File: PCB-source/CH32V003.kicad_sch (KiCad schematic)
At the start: 5 parts, among them J5 Conn_01x03_Pin, U7 CH32V003FxUx

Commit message: Component placement done
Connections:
- no-connect marks 10 -> 11
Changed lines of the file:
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@@
+	)
+	(no_connect
+		(at 147.32 83.82)
 	)
 	(no_connect

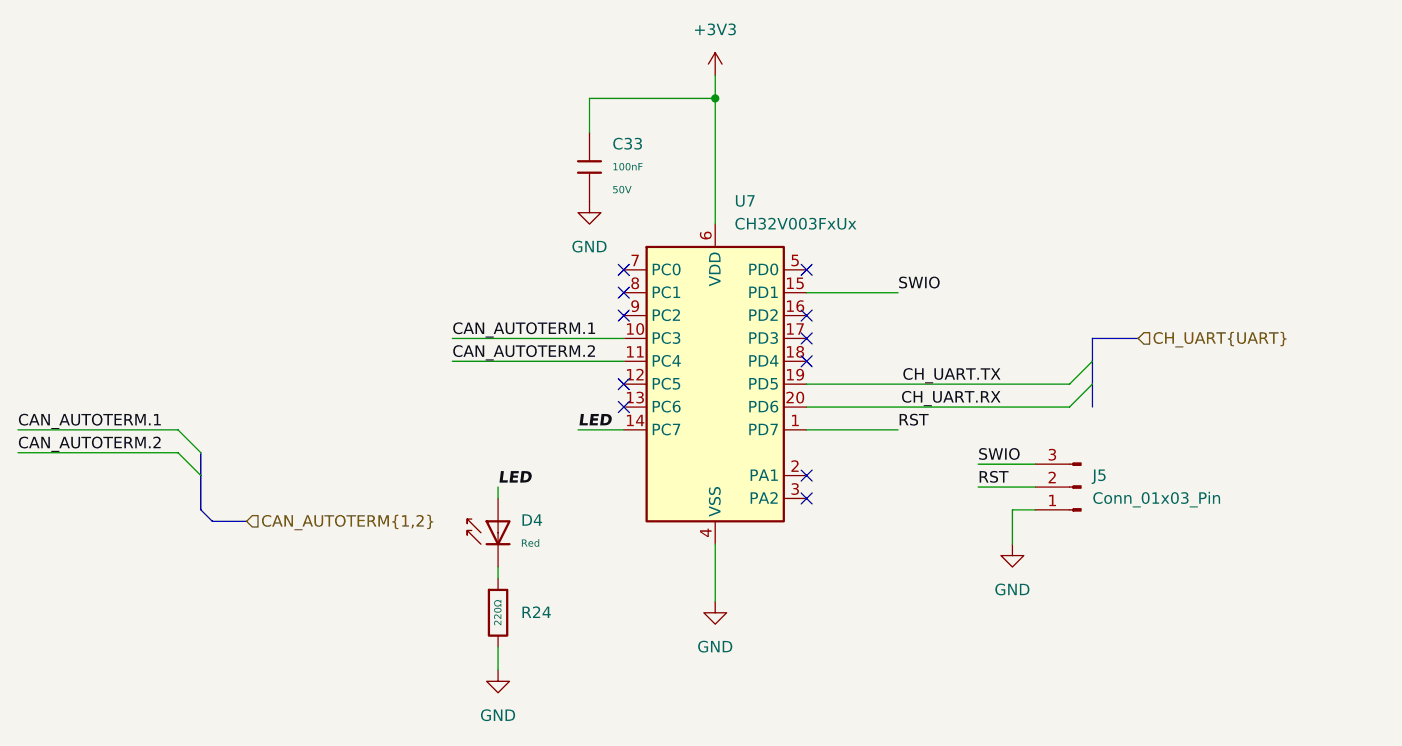
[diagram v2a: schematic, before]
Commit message: change can term add usr led
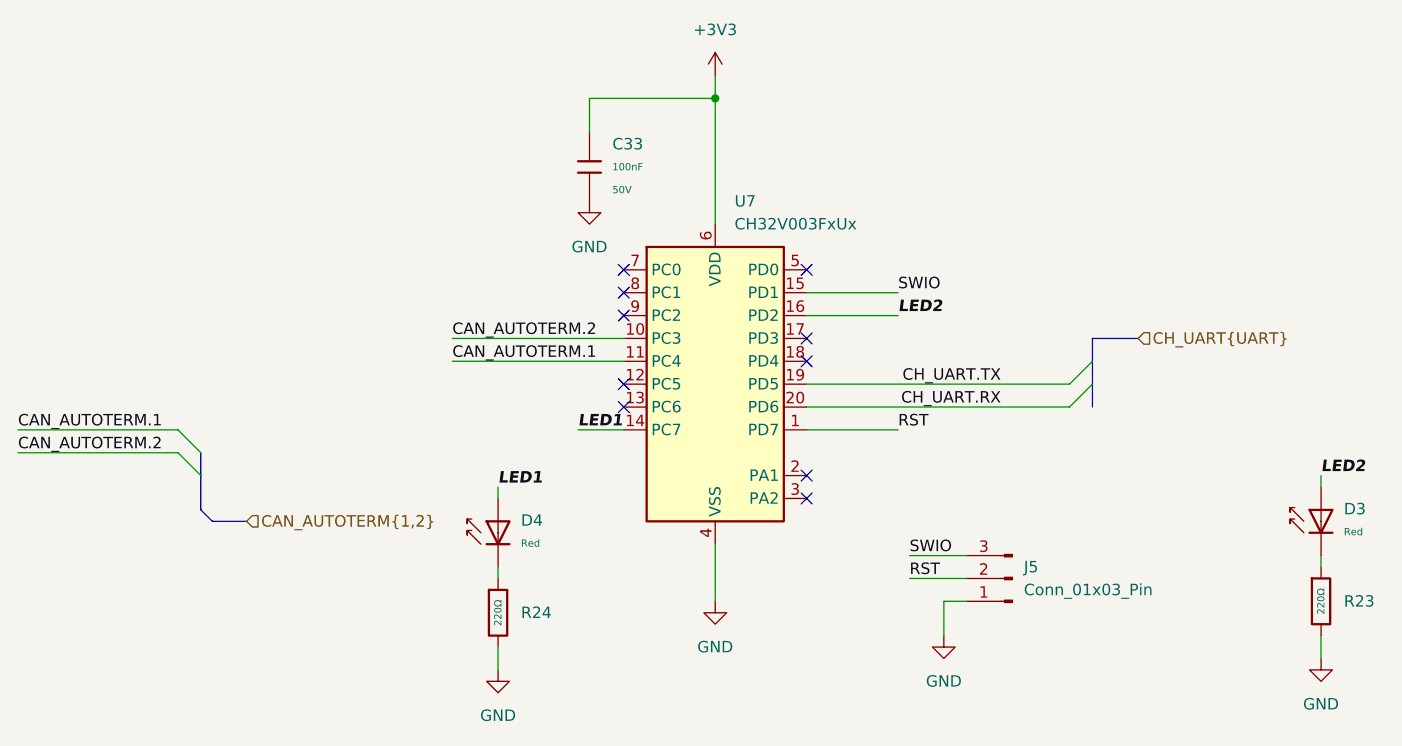
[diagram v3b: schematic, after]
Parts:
- added D3: Red, PCM_JLCPCB:D_0603, symbol PCM_JLCPCB-Diodes:LED,0603,Red
- added R23: 220Ω, PCM_JLCPCB:R_0402, symbol PCM_JLCPCB-Resistors:0402,220Ω
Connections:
- net CAN_AUTOTERM.1: now also U7.11 (PC4); no longer U7.10 (PC3)
- net CAN_AUTOTERM.2: now also U7.10 (PC3); no longer U7.11 (PC4)
- net GND: now also R23.2
- net LED2: now reaches U7.16 (PD2)
- net LED2: now also D3.2
- net LED renamed LED1
- new net: D3.1, R23.1
- no-connect marks 11 -> 10
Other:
- moved on the sheet: J5

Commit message: bom done
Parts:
- J5: now left out of the parts list
- U7: LCSC (none) -> C5299908
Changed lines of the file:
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@@
+			)
+		)
+		(property "LCSC" "C5299908"
+			(at 137.16 91.44 0)
+			(effects
+				(font
+					(size 1.27 1.27)
+				)
+				(hide yes)
 			)
 		)
@@
 		(unit 1)
 		(exclude_from_sim no)
-		(in_bom yes)
+		(in_bom no)
 		(on_board yes)
 		(dnp no)
